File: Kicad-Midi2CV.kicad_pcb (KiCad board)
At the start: 2 copper layers, 99.7 x 99.7 mm, 78 parts, among them IC1 MCP4725module, IC2 MCP4725module, J1 Doepfer connector, J10 CV4, J11 Gate1, J12 GateConn, J13 Gate2, J14 Gate3, J15 Gate4, J16 I2C_Conn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

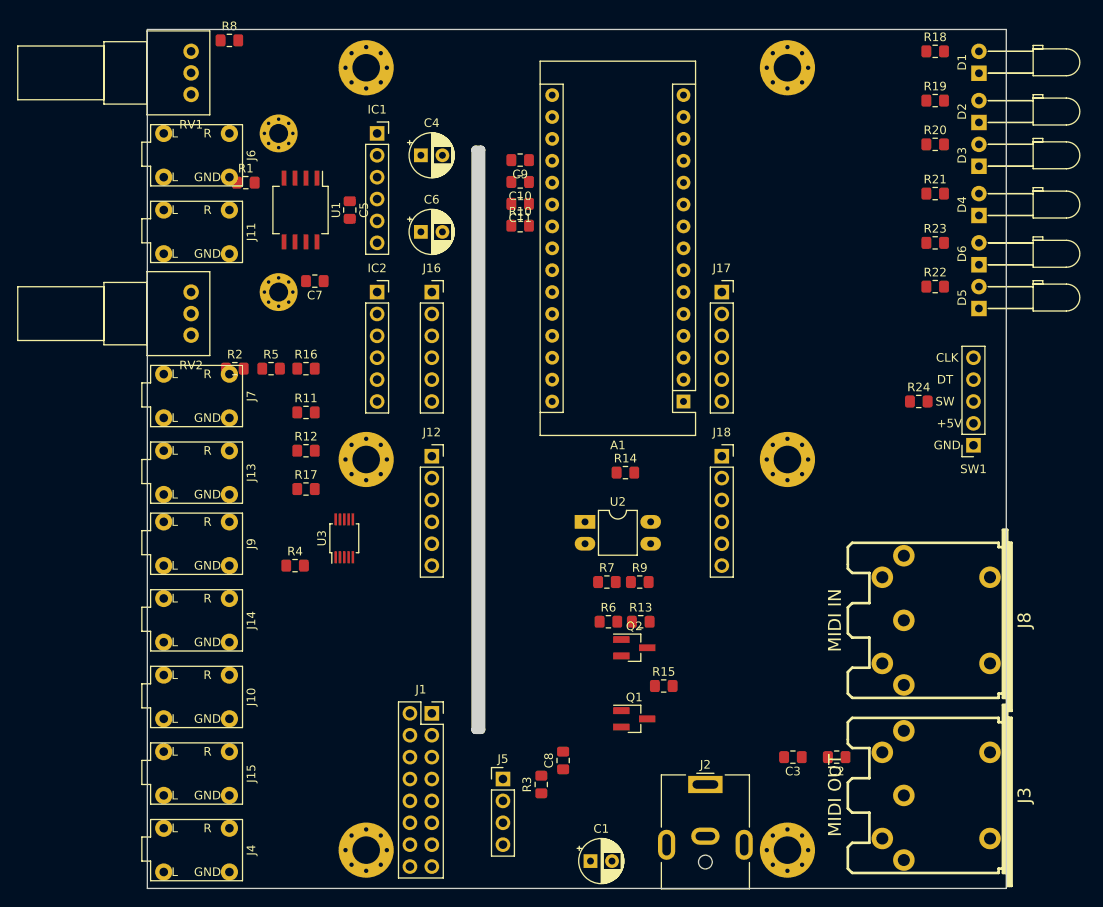
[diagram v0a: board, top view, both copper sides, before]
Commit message: Analogue card routed - no GND
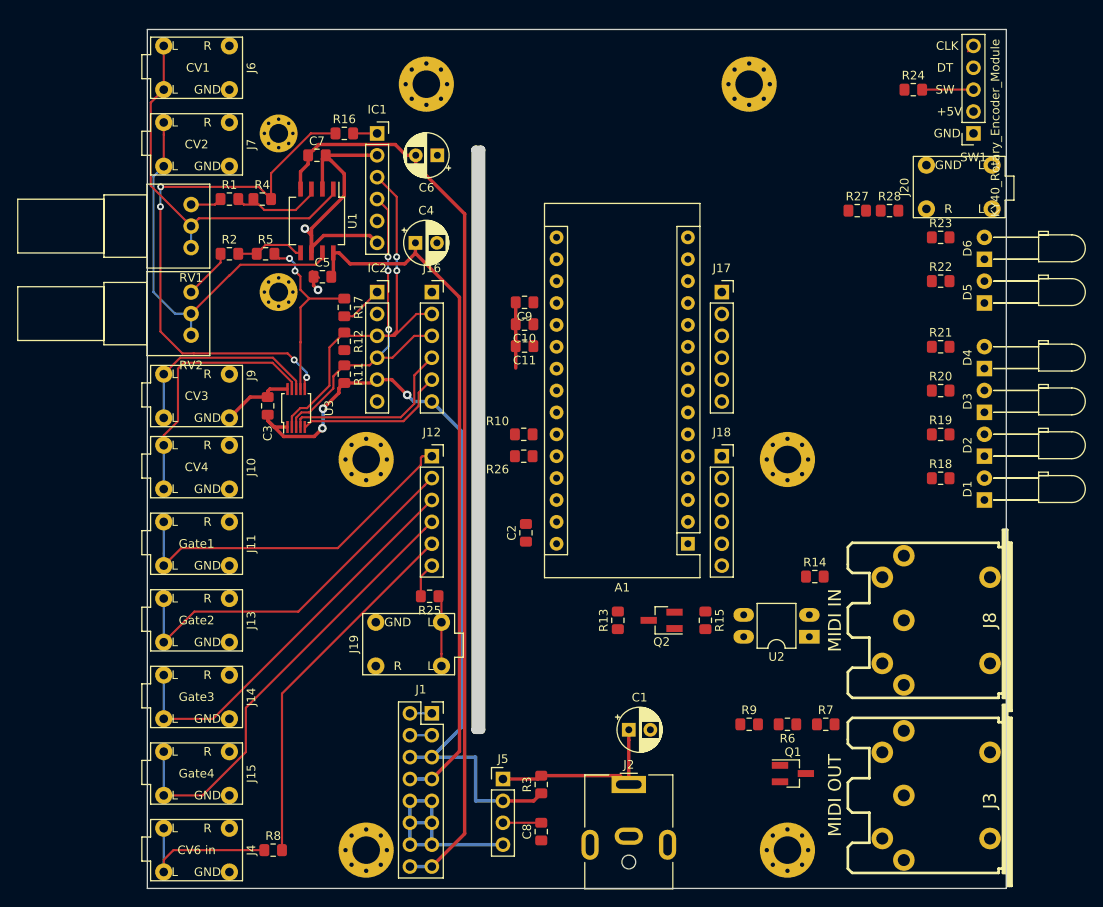
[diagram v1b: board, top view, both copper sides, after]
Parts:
- added J19: CV7 in, Connector_Audio:AudioJack3StereoNarrow-PJ-321, F.Cu at (55.7, 96.7)
- added J20: CV3 in, Connector_Audio:AudioJack3StereoNarrow-PJ-321, F.Cu at (119.6, 43.7)
- added R25: 10k, Resistor_SMD:R_0805_2012Metric_Pad1.15x1.40mm_HandSolder, F.Cu at (58.2, 91.2)
- added R26: 10k, Resistor_SMD:R_0805_2012Metric_Pad1.15x1.40mm_HandSolder, F.Cu at (69.1, 74.9)
- added R27: 10k, Resistor_SMD:R_0805_2012Metric_Pad1.15x1.40mm_HandSolder, F.Cu at (107.8, 46.4)
- added R28: 10k, Resistor_SMD:R_0805_2012Metric_Pad1.15x1.40mm_HandSolder, F.Cu at (111.5, 46.4)
- C8: value C -> 100n
- J4: value CV in -> CV6 in
- moved R8 94.1 mm to (40.0, 120.7)
- moved C3 73.3 mm to (39.4, 69.1), turned to 270 degrees
- moved R18 49.6 mm to (117.5, 77.5)
- moved D1 49.5 mm to (122.6, 80.0)
- moved C2 44.5 mm to (69.3, 83.8), turned to 90 degrees
- moved R4 42.7 mm to (38.7, 45.1)
- moved R19 38.8 mm to (117.5, 72.4)
- moved D2 38.7 mm to (122.6, 74.9)
- moved R24 36.2 mm to (114.3, 32.4)
- moved J11 36.2 mm to (31.1, 85.1)
- moved SW1 36.2 mm to (121.3, 37.5)
- moved R7 30.3 mm to (104.1, 106.0)
- moved U2 29.3 mm to (102.2, 95.9), turned to 180 degrees
- moved J7 29.2 mm to (31.1, 38.7)
- moved R20 28.6 mm to (117.5, 67.3)
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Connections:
- net Net-(IC1-Pad1) renamed /Vout1
- net Net-(IC2-Pad1) renamed /Vout2
- R10 pad 1: GND -> A6
- R10 pad 2: A3 -> GND
- R16 pad 1: CV2 -> CV1
- R17 pad 1: CV1 -> CV2
- R8 pad 2: A3 -> A6
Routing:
- net /-12v: track 0.00 -> 106.8 mm
- net +5V: track 0.00 -> 93.3 mm, vias 0 -> 3
- net /12v: track 0.00 -> 81.7 mm
- net GND: track 0.00 -> 81.1 mm, vias 0 -> 2
- net CV1: track 0.00 -> 63.6 mm, vias 0 -> 4
- net Gate4: track 0.00 -> 52.4 mm
- net Gate3: track 0.00 -> 46.7 mm
- net /SCL: track 0.00 -> 46.6 mm, vias 0 -> 2
- net CV2Gain: track 0.00 -> 46.6 mm
- net CV1Gain: track 0.00 -> 44.6 mm
- net Gate2: track 0.00 -> 44.1 mm
- net A6: track 0.00 -> 42.8 mm
- net Gate1: track 0.00 -> 42.0 mm
- net /SDA: track 0.00 -> 41.1 mm, vias 0 -> 3
- net CV4: track 0.00 -> 29.9 mm
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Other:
- net class Power added: clearance 0.2, trace_width 0.4, via_dia 1, via_drill 0.5

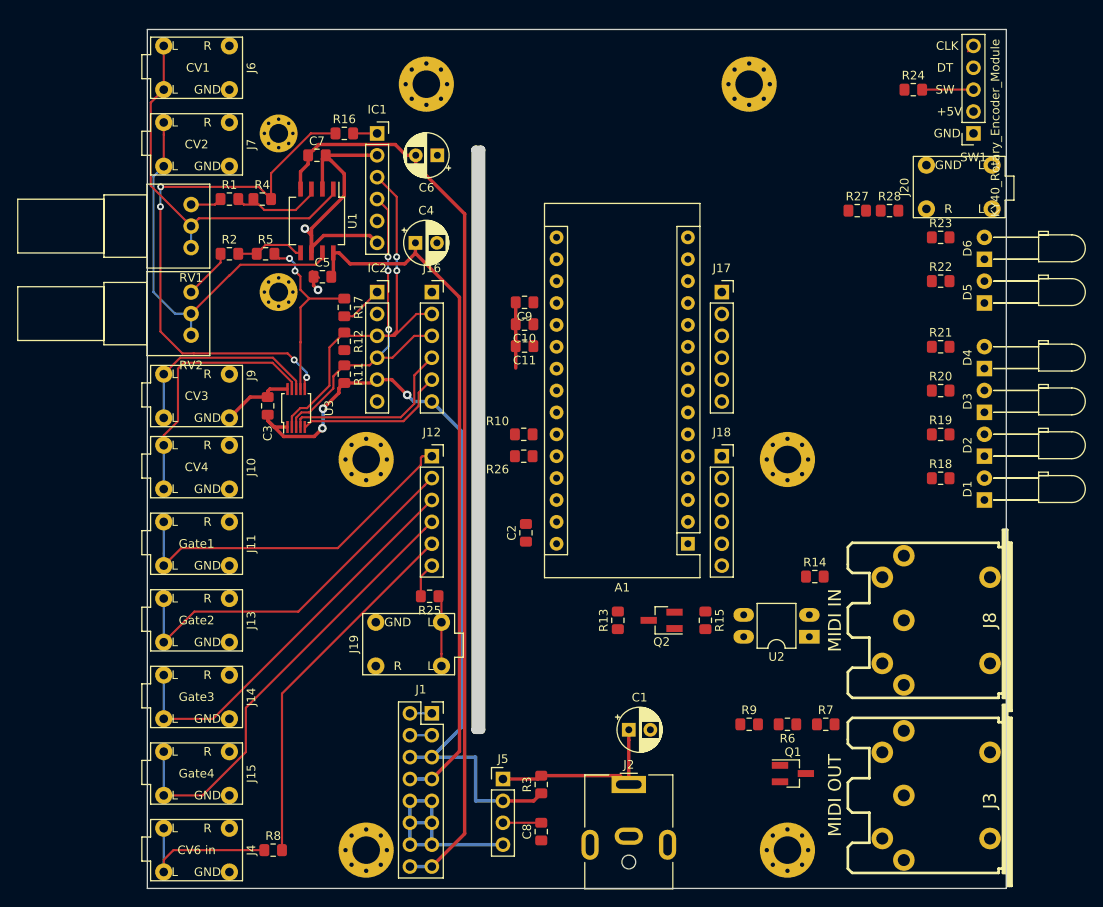
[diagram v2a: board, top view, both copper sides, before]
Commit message: Initial routing on CPU side
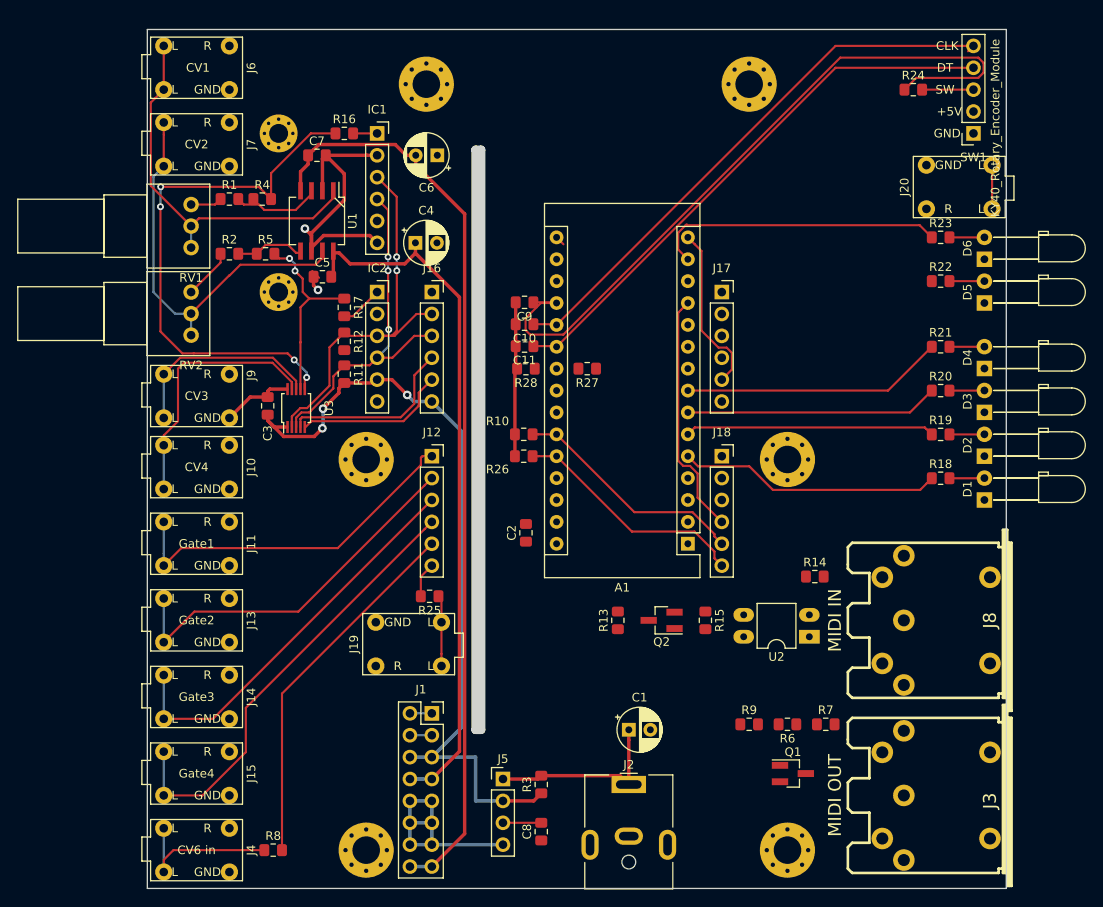
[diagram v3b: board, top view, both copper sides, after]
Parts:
- U1: footprint Package_SO:SO-8_5.3x6.2mm_P1.27mm -> AJ-Dropbox-Kicad:AJ_SO-8_5.3x6.2mm_P1.27mm
- moved R28 46.0 mm to (69.3, 64.8), turned to 180 degrees
- moved R27 36.3 mm to (76.5, 64.8), turned to 180 degrees
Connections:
- R4 pad 2: CV1 -> GND
- R5 pad 2: CV2 -> GND
- U1 pad 2: GND -> Net-(R1-Pad2)
- U1 pad 3: Net-(R1-Pad2) -> CV1
- U1 pad 5: Net-(R2-Pad2) -> CV2
- U1 pad 6: GND -> Net-(R2-Pad2)
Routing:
- net Btn: track 0.00 -> 86.5 mm
- net A2: track 0.00 -> 64.5 mm
- net A1: track 0.90 -> 65.4 mm
- net LED-sel2: track 0.00 -> 34.1 mm
- net LED1: track 0.00 -> 30.5 mm
- net LED4: track 0.00 -> 30.4 mm
- net LED3: track 0.00 -> 29.4 mm
- net LED2: track 0.00 -> 29.0 mm
- net Gate4: track 52.4 -> 80.8 mm
- net A7: track 4.09 -> 31.8 mm
- net A6: track 42.8 -> 70.1 mm
- net /RDY-BSY: track 17.9 -> 37.6 mm
- net GND: track 81.1 -> 91.9 mm
- net Net-(D1-Pad2): track 0.00 -> 5.30 mm
- net Net-(J20-PadT): track 0.00 -> 5.08 mm
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
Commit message: Before planes...
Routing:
- net +5V: track 93.3 -> 191.9 mm, vias 3 -> 6
- net Net-(A1-Pad17): track 4.45 -> 74.2 mm
- net GND: track 91.9 -> 159.6 mm, vias 2 -> 3
- net /LDAC: track 22.2 -> 53.6 mm, vias 0 -> 2
- net /TX: track 0.00 -> 31.1 mm, vias 0 -> 2
- net LED-sel: track 0.00 -> 29.2 mm, vias 0 -> 1
- net Gate3: track 46.7 -> 75.7 mm
- net /SCL: track 46.6 -> 75.5 mm, vias 2 -> 3
- net VCC: track 21.5 -> 50.3 mm
- net /SDA: track 41.1 -> 62.9 mm, vias 3 -> 4
- net Gate2: track 44.1 -> 64.3 mm, vias 0 -> 1
- net /RX: track 0.00 -> 18.0 mm, vias 0 -> 1
- net Gate1: track 42.0 -> 56.5 mm
- net /MIDI-OUT: track 0.00 -> 12.4 mm
- net Net-(J8-Pad5): track 0.00 -> 11.0 mm
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
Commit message: RevA PCB
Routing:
- net Net-(J20-PadT): track 5.08 -> 68.7 mm, vias 0 -> 4
- net +5V: track 191.9 -> 214.5 mm, vias 6 -> 9
- net A3: track 0.00 -> 6.46 mm, vias 0 -> 1
- net CV1: track 63.6 -> 68.6 mm
- net Net-(R2-Pad2): track 8.03 -> 11.0 mm
- net /12v: track 81.7 -> 84.4 mm
- net GND: track 159.6 -> 161.4 mm, vias 3 -> 6
- net LED-sel2: track 36.0 -> 36.8 mm
- net Net-(R1-Pad2): track 10.4 -> 11.1 mm
- added copper zone on F.Cu, net +5V
- added copper zone on B.Cu, net GND

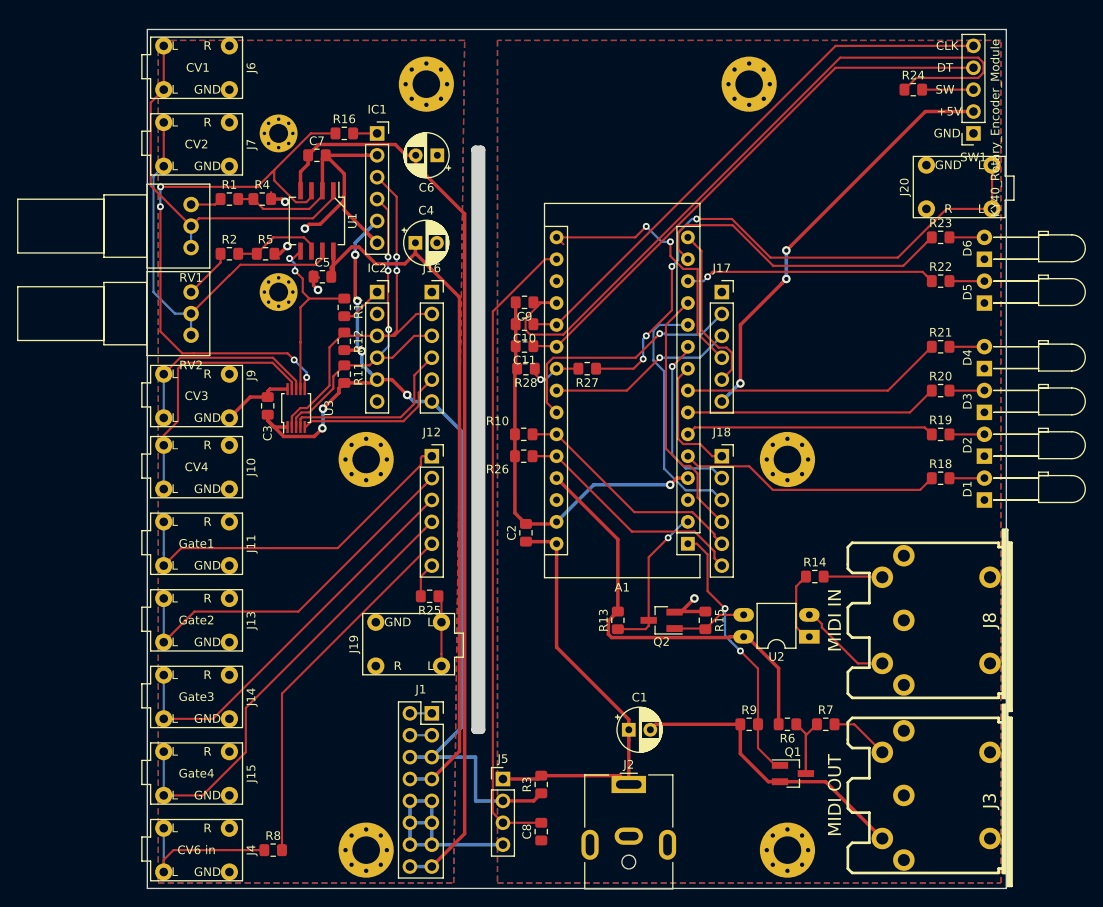
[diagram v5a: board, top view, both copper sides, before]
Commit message: PCB Final Trim
Silk adj:
Text adjustments
Label board x2
Label headers
Add values to resistors on silk

Power lanes beefed up (0,5 or 0,6) when long or feed.
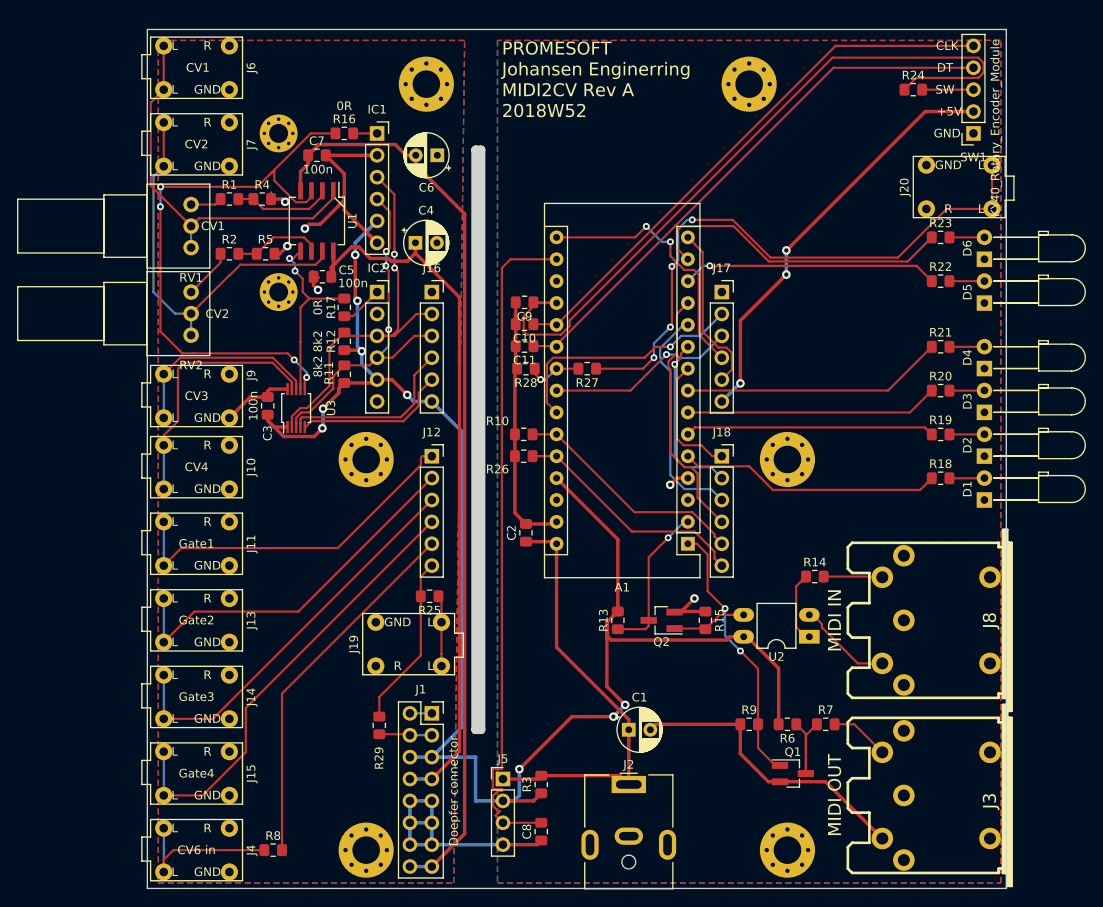
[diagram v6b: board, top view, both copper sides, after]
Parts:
- added R29: 1k, Resistor_SMD:R_0805_2012Metric_Pad1.15x1.40mm_HandSolder, F.Cu at (52.3, 106.2)
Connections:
- net Net-(J1-Pad1) renamed /Gate
- net Net-(J1-Pad3) renamed /CV
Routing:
- net +5V: track 214.5 -> 246.1 mm, vias 9 -> 12
- net A7: track 31.8 -> 47.7 mm
- net GND: track 161.4 -> 147.6 mm
- net Net-(A1-Pad17): track 74.2 -> 79.4 mm
- net /CV: track 2.54 -> 6.14 mm
- net Gate3: track 75.7 -> 73.4 mm
- net /LDAC: track 53.6 -> 52.2 mm
- net Btn: track 86.5 -> 87.5 mm
- net LED-sel: track 29.2 -> 30.1 mm
- net Net-(J20-PadT): track 68.7 -> 69.4 mm
- net /SDA: track 62.9 -> 63.6 mm
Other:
- board text added: "PROMESOFT Johansen Enginerring MIDI2CV Rev A 2018W52"
- board text added: "PROMESOFT Johansen Enginerring SubSection - 2018W52 DAC Gate CV"
- board text added: "Tip + Shield GND"

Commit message: Gerber
Gerber and Drill for JLC
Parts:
- moved R29 0.76 mm to (51.6, 106.2)
- moved D1 0.51 mm to (122.0, 80.0)
- moved D2 0.51 mm to (122.0, 74.9)
- moved D3 0.51 mm to (122.0, 69.8)
- moved D4 0.51 mm to (122.0, 64.8)
- moved D5 0.51 mm to (122.0, 57.1)
- moved D6 0.51 mm to (122.0, 52.1)
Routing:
- net Net-(A1-Pad17): track 79.4 -> 76.7 mm
- net /CV: track 6.14 -> 7.10 mm
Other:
- board text added: "+Vin +5v +3v3 GND"
- board text added: "D6 D7 D8 D9 A6 A7"
- board text added: "G1 G2 G3 G4 CV6 CV7"
- board text added: "G8 CV +5 +12 GND GND GND -12"
- board text added: "GND A5 A4 D12 D13 5V"
- board text added: "GND SCL SDA LDAC RDY +5V"
- board text added: "PROMESOFT Johansen Enginerring SubSection - 2018W52 DAC Gate CV RevA"
- board text removed: "PROMESOFT Johansen Enginerring SubSection - 2018W52 DAC Gate CV"
